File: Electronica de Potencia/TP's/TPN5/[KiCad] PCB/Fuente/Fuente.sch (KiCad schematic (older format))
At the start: 64 parts, among them J1 220 VAC

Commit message: actualizo fuente
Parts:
- removed D?: LED, symbol Device:LED
- added D2: Rojo_5mm, symbol Device:LED_Small
- added D5: Verde_5mm, symbol Device:LED_Small
- added R14: 10k, symbol Device:R_Small_US
- added SW1: ROCKER, lib_fp:Rocker, symbol Switch:SW_DPST_x2
- C17, C19: renamed from C?; value 100n -> 0.1u
- C7: renamed from C?; value 330u|200V -> 330u|24V
- C9: renamed from C?; value 220u|24V -> 330u|24V
- D3: renamed from D?; footprint (none) -> lib_fp:TO-220-3_Vertical
- J2: renamed from J?; footprint (none) -> lib_fp:TerminalBlock_bornier-2_P5.08mm
- MOD1: renamed from MOD?; footprint (none) -> lib_fp:MP1584
- Q1, Q2: renamed from Q?; value Q_NMOS_GDS -> IRF840; footprint (none) -> lib_fp:TO-220-3_Vertical
- R13: renamed from R?; value 1K -> 1,5K
- T1: renamed from T?; footprint (none) -> lib_fp:Transformador_EE25
- U1: renamed from U?; footprint (none) -> Package_DIP:DIP-16_W7.62mm_LongPads
- gave numbers to parts that had none: 30
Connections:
- net labels added: +5V_REF
- net labels removed: +5V_Ref
- wire segments 226 -> 233
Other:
- note added: "ACCESORIOS"
- note added: "ETAPA DE SALIDA"
- moved on the sheet: C1, C10, C11, C12, C13, C14, C15, C16, C17, C18, C19, C2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

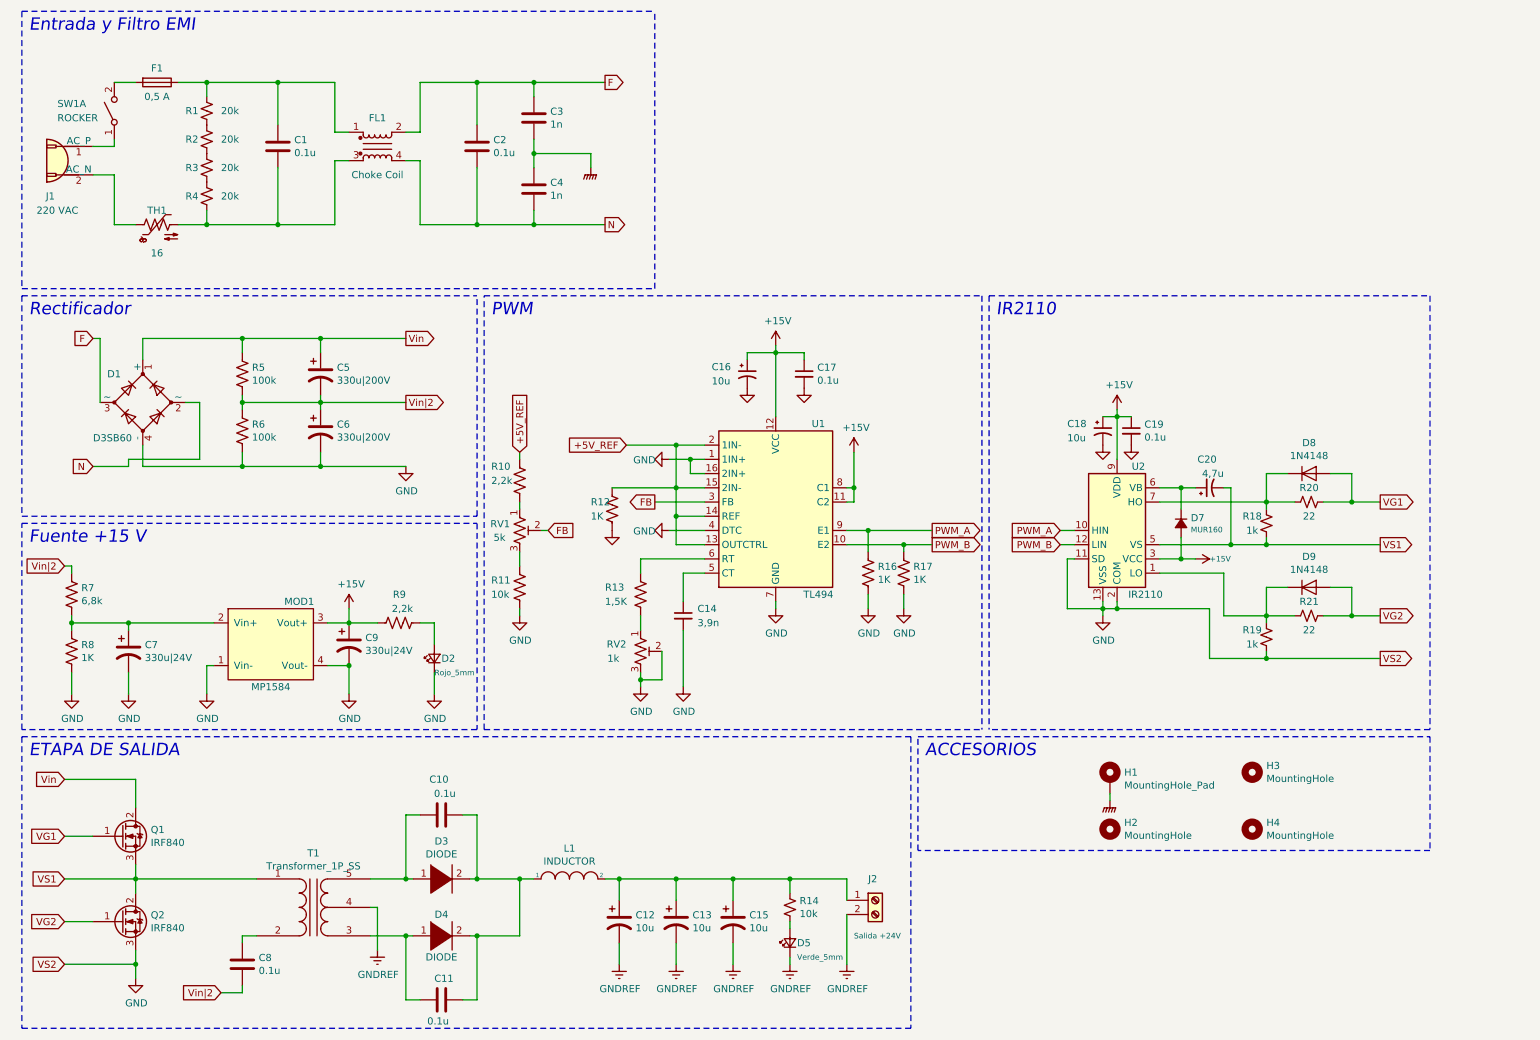
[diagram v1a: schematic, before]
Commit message: Cambio el PCB de la fuente
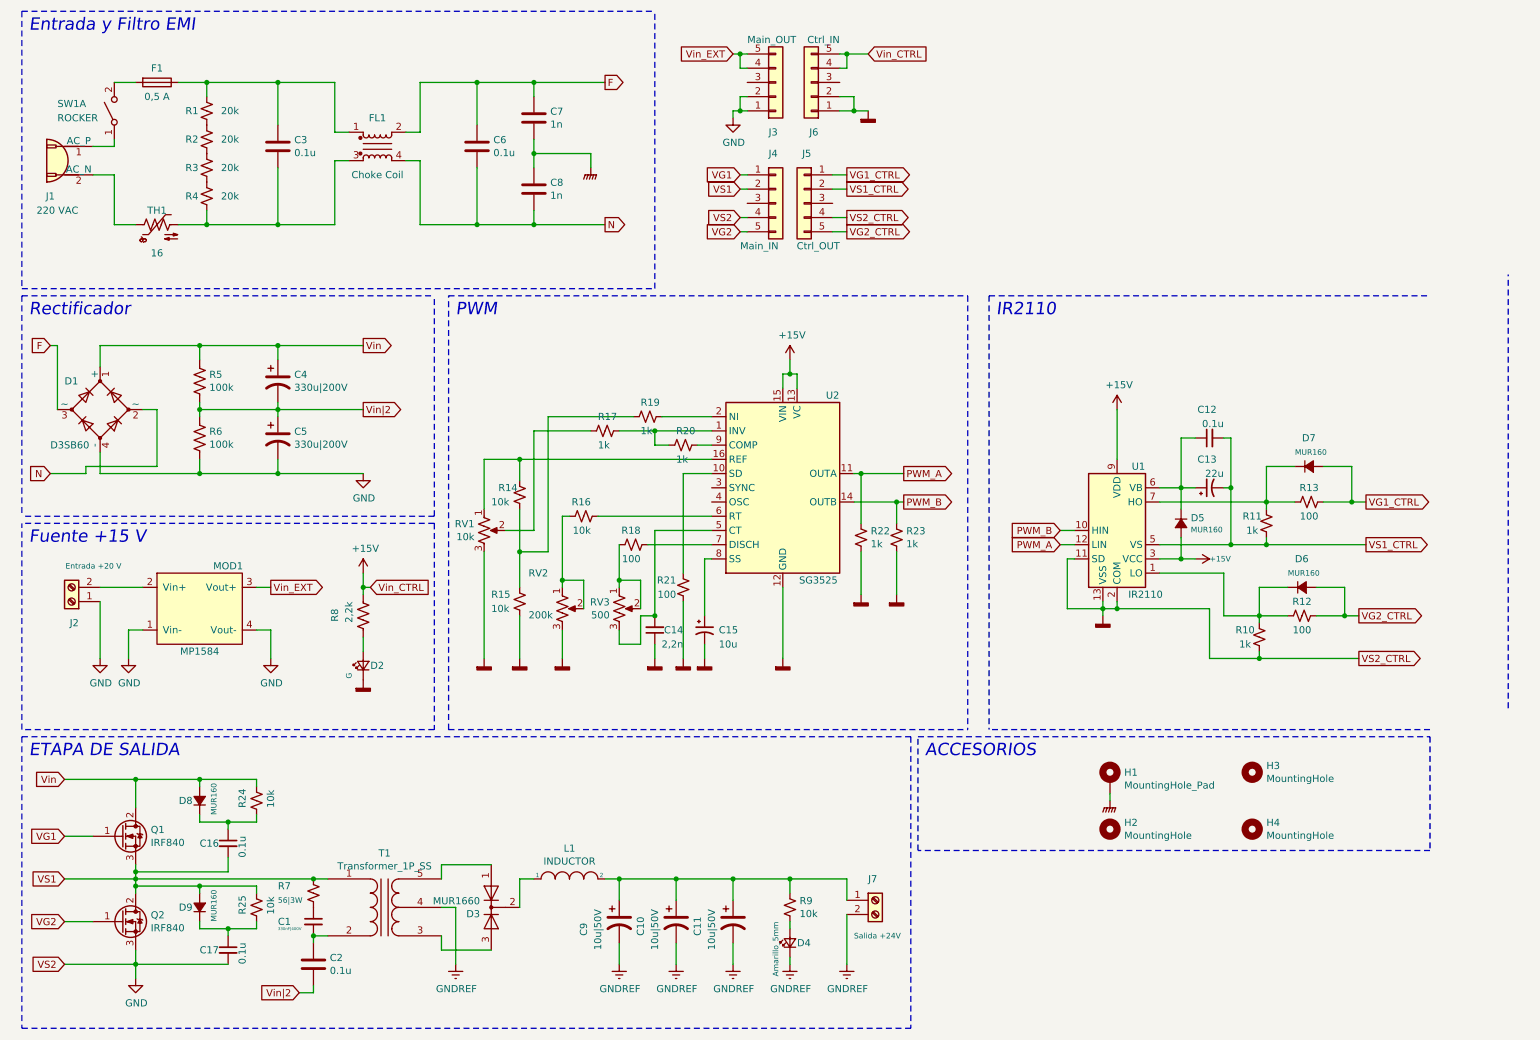
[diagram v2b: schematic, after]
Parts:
- removed C10, C11: 0.1u, Capacitor_THT:C_Rect_L16.5mm_W5.0mm_P15.00mm_MKT, symbol Device:C
- removed C16, C18: 10u, symbol Device:CP1_Small
- removed C19: 0.1u, symbol Device:C_Small
- removed C7, C9: 330u|24V, Capacitor_THT:CP_Radial_D18.0mm_P7.50mm, symbol Device:CP1
- removed D3: DIODE, lib_fp:TO-220-3_Vertical, symbol pspice:DIODE
- removed D4: DIODE, symbol pspice:DIODE
- removed D8, D9: 1N4148, Diode_THT:D_DO-35_SOD27_P7.62mm_Horizontal, symbol Diode:1N4148
- removed R10: 2,2k, Resistor_THT:R_Axial_DIN0411_L9.9mm_D3.6mm_P12.70mm_Horizontal, symbol Device:R_US
- removed R11: 10k, Resistor_THT:R_Axial_DIN0411_L9.9mm_D3.6mm_P12.70mm_Horizontal, symbol Device:R_US
- removed R12, R16, R17, R8: 1K, Resistor_THT:R_Axial_DIN0411_L9.9mm_D3.6mm_P12.70mm_Horizontal, symbol Device:R_US
- removed R13: 1,5K, Resistor_THT:R_Axial_DIN0411_L9.9mm_D3.6mm_P12.70mm_Horizontal, symbol Device:R_US
- removed R7: 6,8k, Resistor_THT:R_Axial_DIN0411_L9.9mm_D3.6mm_P12.70mm_Horizontal, symbol Device:R_US
- removed RV1: 5k, symbol Device:R_POT_TRIM_US
- removed RV2: 1k, symbol Device:R_POT_TRIM_US
- removed U1: TL494, Package_DIP:DIP-16_W7.62mm_LongPads, symbol Regulator_Controller:TL494
- added C1: 330nF|400V, lib_fp:C_Rect_L16.5mm_W5.0mm_P15.00mm_MKT, symbol Device:C_Small
- added C12, C16: 0.1u, lib_fp:C_Disc_D3.8mm_W2.6mm_P2.50mm, symbol Device:C_Small
- added C15: 10u, lib_fp:CP_Radial_D5.0mm_P2.50mm, symbol Device:CP1_Small
- added D3: MUR1660, lib_fp:TO-220-3_Vertical, symbol Device:D_x2_KCom_AKA
- added D6, D7, D8, D9: MUR160, lib_fp:D_DO-41_SOD81_P10.16mm_Horizontal, symbol Device:D_Small_ALT
- added J2: Entrada +20 V, lib_fp:TerminalBlock_bornier-2_P5.08mm, symbol Connector:Screw_Terminal_01x02
- added J3: Main_OUT, Connector_PinSocket_2.54mm:PinSocket_1x05_P2.54mm_Vertical, symbol Connector_Generic:Conn_01x05
- added J4: Main_IN, Connector_PinSocket_2.54mm:PinSocket_1x05_P2.54mm_Vertical, symbol Connector_Generic:Conn_01x05
- added J5: Ctrl_OUT, Connector_PinHeader_2.54mm:PinHeader_1x05_P2.54mm_Vertical, symbol Connector_Generic:Conn_01x05
- added J6: Ctrl_IN, Connector_PinHeader_2.54mm:PinHeader_1x05_P2.54mm_Vertical, symbol Connector_Generic:Conn_01x05
- added R14, R15, R16, R24, R25: 10k, lib_fp:R_Axial_DIN0207_L6.3mm_D2.5mm_P10.16mm_Horizontal, symbol Device:R_Small_US
- added R17, R19, R20, R22, R23: 1k, lib_fp:R_Axial_DIN0207_L6.3mm_D2.5mm_P10.16mm_Horizontal, symbol Device:R_Small_US
- added R18: 100, lib_fp:R_Axial_DIN0204_L3.6mm_D1.6mm_P5.08mm_Horizontal, symbol Device:R_Small_US
- added R21: 100, lib_fp:R_Axial_DIN0207_L6.3mm_D2.5mm_P10.16mm_Horizontal, symbol Device:R_Small_US
- added R7: 56|3W, lib_fp:R_Axial_DIN0617_L17.0mm_D6.0mm_P20.32mm_Horizontal, symbol Device:R_Small_US
- added RV1: 10k, lib_fp:Potentiometer_Bourns_3266Y_Vertical, symbol Device:R_POT_US
- added RV2: 200k, lib_fp:Potentiometer_Bourns_3266Y_Vertical, symbol Device:R_POT_US
- added RV3: 500, lib_fp:Potentiometer_Bourns_3266Y_Vertical, symbol Device:R_POT_US
- added U2: SG3525, lib_fp:DIP-16_W7.62mm_LongPads, symbol Regulator_Controller:SG3525
- C10: renamed from C13; value 10u -> 10u|50V; footprint Capacitor_THT:CP_Radial_D18.0mm_P7.50mm -> lib_fp:CP_Radial_D5.0mm_P2.50mm
- C11: renamed from C15; value 10u -> 10u|50V; footprint Capacitor_THT:CP_Radial_D18.0mm_P7.50mm -> lib_fp:CP_Radial_D5.0mm_P2.50mm
- C13: renamed from C20; value 4,7u -> 22u; footprint (none) -> lib_fp:CP_Radial_D5.0mm_P2.50mm
- C14: value 3,9n -> 2,2n; footprint (none) -> lib_fp:C_Disc_D3.8mm_W2.6mm_P2.50mm
- C17: footprint (none) -> lib_fp:C_Disc_D3.8mm_W2.6mm_P2.50mm
- C2: renamed from C8; footprint Capacitor_THT:C_Rect_L16.5mm_W5.0mm_P15.00mm_MKT -> lib_fp:C_Rect_L16.5mm_W5.0mm_P15.00mm_MKT
- C3: renamed from C1; footprint Capacitor_THT:C_Rect_L16.5mm_W5.0mm_P15.00mm_MKT -> lib_fp:C_Rect_L16.5mm_W5.0mm_P15.00mm_MKT
- C4: renamed from C5; footprint Capacitor_THT:CP_Radial_D18.0mm_P7.50mm -> Capacitor_THT:CP_Radial_D25.0mm_P10.00mm_SnapIn
- C5: renamed from C6; footprint Capacitor_THT:CP_Radial_D18.0mm_P7.50mm -> Capacitor_THT:CP_Radial_D25.0mm_P10.00mm_SnapIn
- C6: renamed from C2; footprint Capacitor_THT:C_Rect_L16.5mm_W5.0mm_P15.00mm_MKT -> lib_fp:C_Rect_L16.5mm_W5.0mm_P15.00mm_MKT
- C9: renamed from C12; value 10u -> 10u|50V; footprint Capacitor_THT:CP_Radial_D18.0mm_P7.50mm -> lib_fp:CP_Radial_D5.0mm_P2.50mm
- D2: value Rojo_5mm -> G; footprint (none) -> lib_fp:LED_D5.0mm_Clear
- D4: renamed from D5; value Verde_5mm -> Amarillo_5mm; footprint (none) -> lib_fp:LED_D5.0mm_Clear
- D5: renamed from D7; footprint (none) -> lib_fp:D_DO-41_SOD81_P10.16mm_Horizontal
- F1: footprint lib_fp:fuse_4pin_A -> lib_fp:Fuse_4pin_A
- H1: footprint MountingHole:MountingHole_3.2mm_M3_DIN965_Pad -> lib_fp:MountingHole_3.2mm_M3_DIN965_Pad
- H2, H3, H4: footprint MountingHole:MountingHole_3.2mm_M3_DIN965 -> lib_fp:MountingHole_3.2mm_M3_DIN965
- L1: footprint (none) -> lib_fp:L_Toroid_Vertical_L22.4mm_W10.2mm_P7.90mm_Vishay_TJ4
- R1, R2, R3, R4: footprint Resistor_SMD:R_0805_2012Metric_Pad1.15x1.40mm_HandSolder -> lib_fp:R_0805_2012Metric_Pad1.15x1.40mm_HandSolder
- R10: renamed from R19; footprint (none) -> lib_fp:R_Axial_DIN0207_L6.3mm_D2.5mm_P10.16mm_Horizontal
- R11: renamed from R18; footprint (none) -> lib_fp:R_Axial_DIN0207_L6.3mm_D2.5mm_P10.16mm_Horizontal
- R12: renamed from R21; value 22 -> 100; footprint (none) -> lib_fp:R_Axial_DIN0207_L6.3mm_D2.5mm_P10.16mm_Horizontal
- R13: renamed from R20; value 22 -> 100; footprint (none) -> lib_fp:R_Axial_DIN0207_L6.3mm_D2.5mm_P10.16mm_Horizontal
- R5, R6: footprint Resistor_THT:R_Axial_DIN0411_L9.9mm_D3.6mm_P12.70mm_Horizontal -> lib_fp:R_Axial_DIN0207_L6.3mm_D2.5mm_P10.16mm_Horizontal
- R8: renamed from R9; footprint Resistor_THT:R_Axial_DIN0411_L9.9mm_D3.6mm_P12.70mm_Horizontal -> lib_fp:R_Axial_DIN0207_L6.3mm_D2.5mm_P10.16mm_Horizontal
- R9: renamed from R14; footprint (none) -> lib_fp:R_Axial_DIN0207_L6.3mm_D2.5mm_P10.16mm_Horizontal
- U1: renamed from U2; footprint Package_DIP:DIP-14_W7.62mm -> lib_fp:DIP-14_W7.62mm_LongPads
- renumbered C3 to C7, C4 to C8, J2 to J7
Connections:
- net +15V: now also R8.2, J6.4 (Pin_4), J6.5 (Pin_5), U2.13 (VC), U2.15 (VIN); no longer C17.1, MOD1.3 (Vout+), R8.1
- net GND: now also J2.1 (Pin_1), J3.1 (Pin_1), J3.2 (Pin_2), J4.4 (Pin_4); no longer C14.2, D2.1 (K), R10.1, U1.11 (SD), U1.13 (VSS), U1.2 (COM)
- net PWM_A: now also U1.12 (LIN), R22.1, U2.11 (OUTA); no longer U1.10 (HIN)
- net PWM_B: now also U1.10 (HIN), R23.1, U2.14 (OUTB); no longer U1.12 (LIN)
- net VG1: now also J4.1 (Pin_1); no longer R13.2
- net VG2: now also J4.5 (Pin_5); no longer R12.2
- net VS1: now also C16.2, D9.2 (A), J4.2 (Pin_2), R25.1, R7.1; no longer C13.2, R11.1, U1.5 (VS)
- net Vin: now also D8.2 (A), R24.1
- net at MOD1.2 (Vin+): now also J2.2 (Pin_2)
- net at D2.2 (A): now also R8.1; no longer R8.2
- net at R10.2, R12.1, U1.1 (LO): now also D6.1 (K)
- net at C13.1, D5.1 (K), U1.6 (VB): now also C12.1
- net at R11.2, R13.1, U1.7 (HO): now also D7.1 (K)
- net GNDD: now reaches C14.1
- net GNDD: now also D2.1 (K), R10.1, U1.11 (SD), U1.13 (VSS), U1.2 (COM), C15.2, J5.4 (Pin_4), J6.1 (Pin_1), J6.2 (Pin_2), R15.2, R21.1, R22.2, R23.2, RV1.3, RV2.3, U2.12 (GND)
- net at C2.1, T1.2 (AB): now also C1.2
- net at T1.3 (SA): now also D3.3 (A)
- net at T1.5 (SB): now also D3.1 (A)
- net at L1.1: now also D3.2 (K)
- new net: C16.1, D8.1 (K), R24.2
- new net: R17.1, R20.2, U2.1 (INV)
- new net: R21.2, U2.10 (SD)
- new net: R14.1, RV1.1, U2.16 (REF)
- new net: R19.1, U2.2 (NI)
- new net: C14.2, RV3.3, U2.5 (CT)
- new net: R16.2, U2.6 (RT)
- new net: R18.2, U2.7 (DISCH)
- new net: C15.1, U2.8 (SS)
- new net: R20.1, U2.9 (COMP)
- new net: C17.1, D9.1 (K), R25.2
- new net: C1.1, R7.2
- new net: R17.2, RV1.2
- new net: R18.1, RV3.1, RV3.2
- new net: R16.1, RV2.1, RV2.2
- new net: R14.2, R15.1, R19.2
- new net VG1_CTRL: D7.2 (A), J5.1 (Pin_1), R13.2
- new net VG2_CTRL: D6.2 (A), J5.5 (Pin_5), R12.2
- new net VS1_CTRL: C12.2, C13.2, J5.2 (Pin_2), R11.1, U1.5 (VS)
- new net Vin_EXT: J3.4 (Pin_4), J3.5 (Pin_5), MOD1.3 (Vout+)
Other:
- moved on the sheet: C2, C4, C5, D1, D2, MOD1, R10, R12, R5, R6, R8, T1

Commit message: Actualizo desde Envy
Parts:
- C1, C12, C14, C16, C17: symbol Device:C_Small -> Fuente-rescue:C_Small-Device
- C10, C11, C9: symbol Device:CP1 -> Fuente-rescue:CP1-Device
- C13, C15: symbol Device:CP1_Small -> Fuente-rescue:CP1_Small-Device
- C2, C3, C6, C7, C8: symbol Device:C -> Fuente-rescue:C-Device
- C4, C5: value 330u|200V -> 470u|200V; symbol Device:CP1 -> Fuente-rescue:CP1-Device
- D1: symbol Device:D_Bridge_+AA- -> Fuente-rescue:D_Bridge_+AA--Device
- D2, D4: symbol Device:LED_Small -> Fuente-rescue:LED_Small-Device
- D3: symbol Device:D_x2_KCom_AKA -> Fuente-rescue:D_x2_KCom_AKA-Device
- D5, D6, D7, D8, D9: symbol Device:D_Small_ALT -> Fuente-rescue:D_Small_ALT-Device
- F1: symbol Device:Fuse -> Fuente-rescue:Fuse-Device
- FL1: symbol Device:EMI_Filter_CommonMode -> Fuente-rescue:EMI_Filter_CommonMode-Device
- H1: symbol Mechanical:MountingHole_Pad -> Fuente-rescue:MountingHole_Pad-Mechanical
- H2, H3, H4: symbol Mechanical:MountingHole -> Fuente-rescue:MountingHole-Mechanical
- J1: symbol Connector:Conn_WallSocket -> Fuente-rescue:Conn_WallSocket-Connector
- J2, J7: symbol Connector:Screw_Terminal_01x02 -> Fuente-rescue:Screw_Terminal_01x02-Connector
- J3, J4, J5, J6: symbol Connector_Generic:Conn_01x05 -> Fuente-rescue:Conn_01x05-Connector_Generic
- L1: symbol pspice:INDUCTOR -> Fuente-rescue:INDUCTOR-pspice
- Q1, Q2: symbol Device:Q_NMOS_GDS -> Fuente-rescue:Q_NMOS_GDS-Device
- R1, R10, R11, R12, R13, R14, R15, R16, R17, R18, R19, R2, R20, R21, R22, R23, R24, R25, R3, R4, R7, R9: symbol Device:R_Small_US -> Fuente-rescue:R_Small_US-Device
- R5, R6, R8: symbol Device:R_US -> Fuente-rescue:R_US-Device
- RV1, RV3: symbol Device:R_POT_US -> Fuente-rescue:R_POT_US-Device
- RV2: value 200k -> 10k; symbol Device:R_POT_US -> Fuente-rescue:R_POT_US-Device
- SW1: symbol Switch:SW_DPST_x2 -> Fuente-rescue:SW_DPST_x2-Switch
- T1: symbol Device:Transformer_1P_SS -> Fuente-rescue:Transformer_1P_SS-Device
- TH1: symbol Device:Thermistor_NTC_US -> Fuente-rescue:Thermistor_NTC_US-Device
- U1: symbol Driver_FET:IR2110 -> Fuente-rescue:IR2110-Driver_FET
- U2: symbol Regulator_Controller:SG3525 -> Fuente-rescue:SG3525-Regulator_Controller
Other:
- moved on the sheet: R17, R19
